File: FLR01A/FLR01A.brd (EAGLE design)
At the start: 30.5 x 30.5 mm, 10 parts, among them J1 M10SMD_MALE, J2 M10SMD_MALE

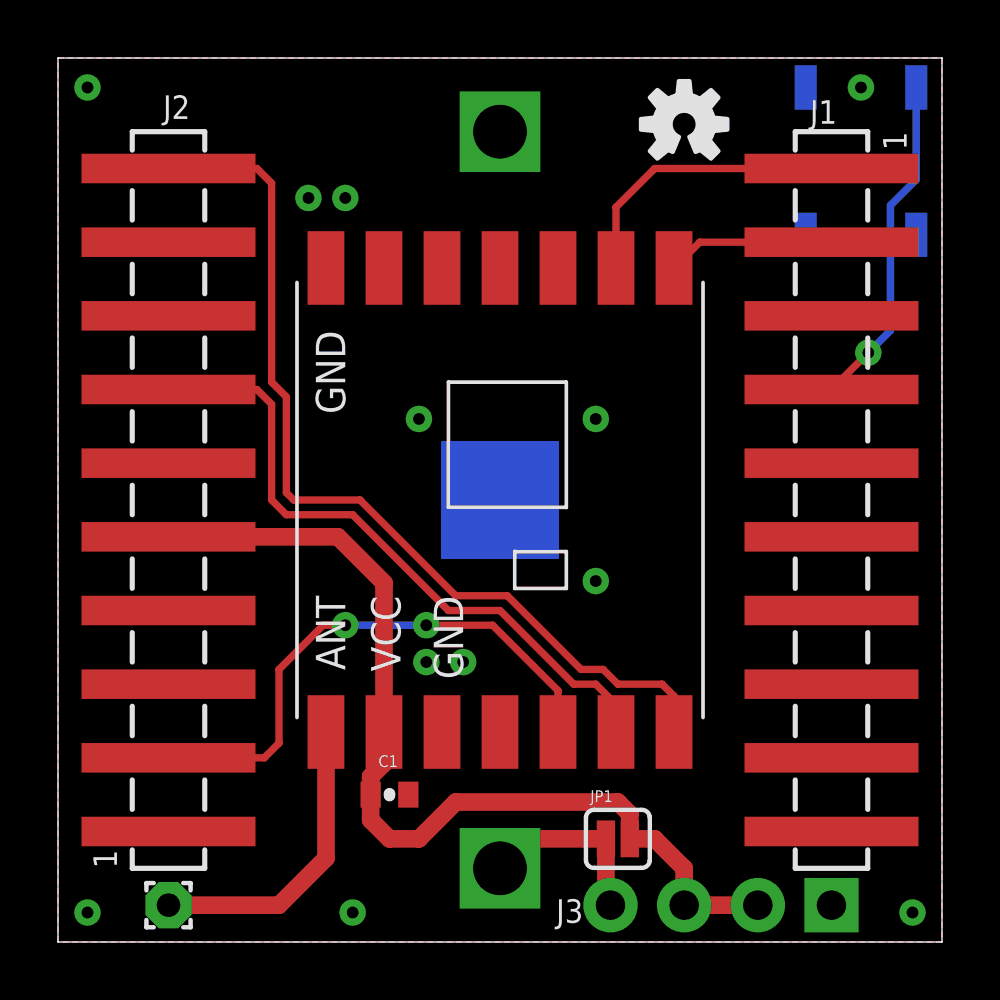
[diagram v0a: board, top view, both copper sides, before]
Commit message: [flr] add ptc fuse in series with battery
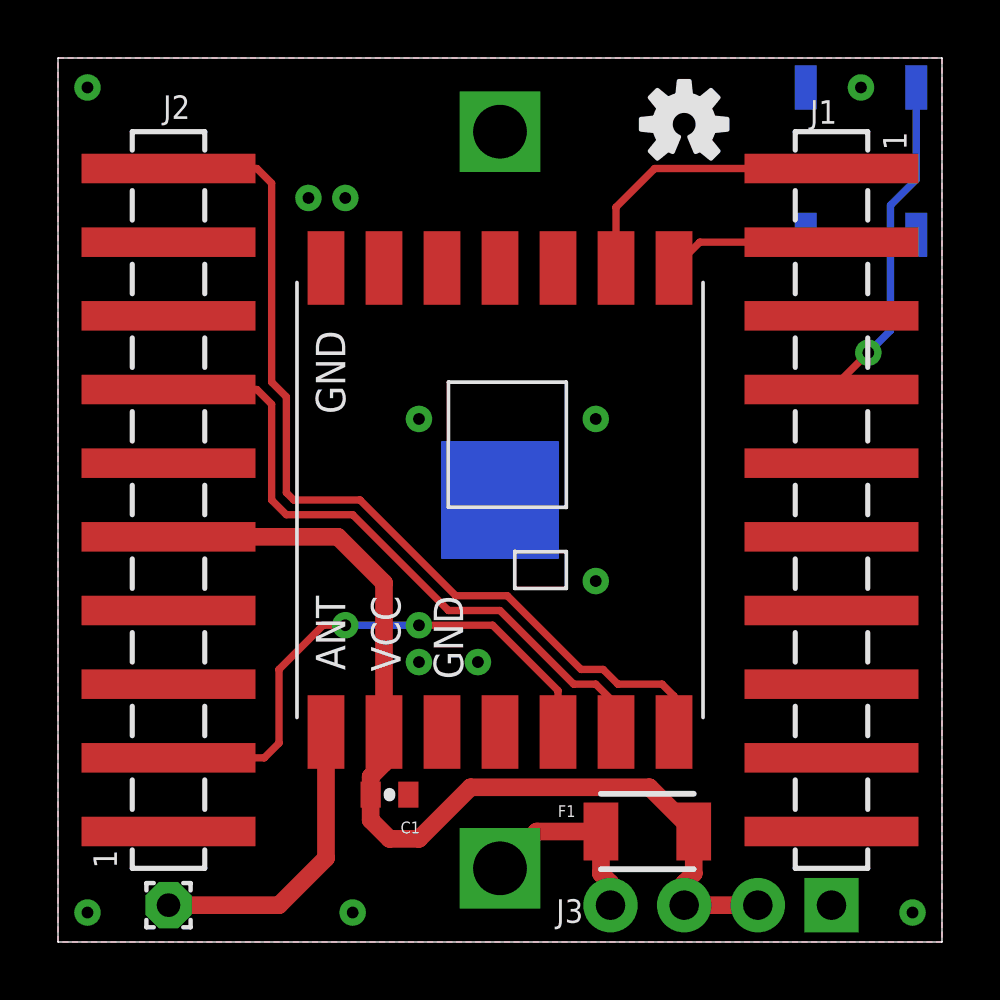
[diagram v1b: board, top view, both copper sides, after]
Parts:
- removed JP1: (no value), SparkFun-Passives:SJ_2S
- added F1: PTC1210, flukso:1210
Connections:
- net 3.3V: now also F1.2; no longer JP1.2
- net N$1: now also F1.1; no longer JP1.1
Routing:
- net 3.3V: track 33.3 -> 34.4 mm
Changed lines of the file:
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@@
 <element name="U$1" library="sparkFun" package="OSHW-LOGO-S" value="OSHW-LOGOS" x="21.59" y="28.194"/>
 <element name="C1" library="sparkFun" package="0402-CAP" value="100nF" x="11.43" y="5.08" smashed="yes">
-<attribute name="NAME" x="11.049" y="6.0325" size="0.4064" layer="25"/>
+<attribute name="NAME" x="11.811" y="3.7465" size="0.4064" layer="25"/>
 </element>
 <element name="U$5" library="flukso" package="RFM12B" value="RFM12B" x="15.24" y="15.24" smashed="yes" rot="R270"/>
@@
 </element>
 <element name="BAT1" library="SparkFun-Electromechanical" package="BATTCON_245MM_PTH" value="" x="15.24" y="15.24" smashed="yes" rot="MR270">
-<attribute name="NAME" x="14.605" y="18.161" size="0.4064" layer="26" rot="MR180"/>
 <attribute name="VALUE" x="15.875" y="24.765" size="0.4064" layer="28" rot="MR270"/>
 </element>
-<element name="JP1" library="SparkFun-Passives" package="SJ_2S" value="" x="19.304" y="3.556"/>
 <element name="J3" library="SparkFun-Connectors" package="1X04_NO_SILK" value="" x="26.67" y="1.27" smashed="yes" rot="R180">
 <attribute name="NAME" x="18.1102" y="1.4732" size="0.8128" layer="25" ratio="10" rot="R180"/>
@@
 <attribute name="PROD_ID" value="SWCH-08247" x="27.686" y="26.924" size="1.778" layer="28" rot="MR270" display="off"/>
 <attribute name="NAME" x="24.384" y="27.559" size="0.4064" layer="26" rot="MR90"/>
+</element>
+<element name="F1" library="flukso" package="1210" value="PTC1210" x="20.32" y="3.81" smashed="yes">
+<attribute name="NAME" x="17.234" y="4.31" size="0.4064" layer="25"/>
 </element>
 </elements>
@@
 <contactref element="BAT1" pad="2"/>
 <contactref element="J3" pad="1"/>
-<via x="12.7" y="9.652" extent="1-16" drill="0.4064" diameter="0.6096"/>
-<via x="13.97" y="9.652" extent="1-16" drill="0.4064" diameter="0.6096"/>
+<via x="12.446" y="9.652" extent="1-16" drill="0.4064" diameter="0.6096"/>
+<via x="14.478" y="9.652" extent="1-16" drill="0.4064" diameter="0.6096"/>
 <via x="8.636" y="25.654" extent="1-16" drill="0.4064" diameter="0.6096"/>
 <via x="9.906" y="25.654" extent="1-16" drill="0.4064" diameter="0.6096"/>
@@
 <contactref element="U$5" pad="VDD"/>
 <contactref element="C1" pad="1"/>
-<contactref element="JP1" pad="2"/>
 <contactref element="J3" pad="3"/>
 <contactref element="J3" pad="2"/>
-<wire x1="19.7159" y1="3.556" x2="19.7159" y2="4.4141" width="0.6096" layer="1"/>
-<wire x1="19.7159" y1="4.4141" x2="19.304" y2="4.826" width="0.6096" layer="1"/>
-<wire x1="19.304" y1="4.826" x2="13.716" y2="4.826" width="0.6096" layer="1"/>
-<wire x1="19.7159" y1="3.556" x2="20.574" y2="3.556" width="0.6096" layer="1"/>
-<wire x1="20.574" y1="3.556" x2="21.59" y2="2.54" width="0.6096" layer="1"/>
-<wire x1="21.59" y1="2.54" x2="21.59" y2="1.27" width="0.6096" layer="1"/>
 <wire x1="21.59" y1="1.27" x2="24.13" y2="1.27" width="0.6096" layer="1"/>
 <wire x1="11.24" y1="7.24" x2="11.24" y2="12.382" width="0.6096" layer="1"/>
 <wire x1="11.24" y1="12.382" x2="9.652" y2="13.97" width="0.6096" layer="1"/>
 <wire x1="9.652" y1="13.97" x2="3.81" y2="13.97" width="0.6096" layer="1"/>
-<wire x1="13.716" y1="4.826" x2="12.446" y2="3.556" width="0.6096" layer="1"/>
+<wire x1="14.224" y1="5.334" x2="12.446" y2="3.556" width="0.6096" layer="1"/>
 <wire x1="12.446" y1="3.556" x2="11.43" y2="3.556" width="0.6096" layer="1"/>
 <wire x1="11.43" y1="3.556" x2="10.78" y2="4.206" width="0.6096" layer="1"/>
@@
 <wire x1="10.78" y1="5.7" x2="11.24" y2="6.16" width="0.6096" layer="1"/>
 <wire x1="11.24" y1="6.16" x2="11.24" y2="7.24" width="0.6096" layer="1"/>
+<contactref element="F1" pad="2"/>
+<wire x1="21.92" y1="3.81" x2="21.92" y2="2.362" width="0.6096" layer="1"/>
+<wire x1="21.92" y1="2.362" x2="21.59" y2="2.032" width="0.6096" layer="1"/>
+<wire x1="21.59" y1="2.032" x2="21.59" y2="1.27" width="0.6096" layer="1"/>
+<wire x1="14.224" y1="5.334" x2="20.396" y2="5.334" width="0.6096" layer="1"/>
+<wire x1="20.396" y1="5.334" x2="21.92" y2="3.81" width="0.6096" layer="1"/>
 </signal>
 <signal name="N$6">
@@
 <wire x1="7.62" y1="6.858" x2="7.62" y2="9.398" width="0.254" layer="1"/>
 <via x="9.906" y="10.922" extent="1-16" drill="0.4064" diameter="0.6096"/>
-<wire x1="9.906" y1="10.922" x2="12.7" y2="10.922" width="0.254" layer="16"/>
-<via x="12.7" y="10.922" extent="1-16" drill="0.4064" diameter="0.6096"/>
+<wire x1="9.906" y1="10.922" x2="12.446" y2="10.922" width="0.254" layer="16"/>
+<via x="12.446" y="10.922" extent="1-16" drill="0.4064" diameter="0.6096"/>
 <wire x1="7.62" y1="9.398" x2="9.144" y2="10.922" width="0.254" layer="1"/>
 <wire x1="9.144" y1="10.922" x2="9.906" y2="10.922" width="0.254" layer="1"/>
-<wire x1="12.7" y1="10.922" x2="14.986" y2="10.922" width="0.254" layer="1"/>
+<wire x1="12.446" y1="10.922" x2="14.986" y2="10.922" width="0.254" layer="1"/>
 <wire x1="14.986" y1="10.922" x2="17.24" y2="8.668" width="0.254" layer="1"/>
 <wire x1="17.24" y1="8.668" x2="17.24" y2="7.24" width="0.254" layer="1"/>
@@
 <contactref element="BAT1" pad="3"/>
 <contactref element="J3" pad="4"/>
-<contactref element="JP1" pad="1"/>
-<wire x1="15.24" y1="2.54" x2="16.256" y2="3.556" width="0.6096" layer="1"/>
-<wire x1="16.256" y1="3.556" x2="18.8921" y2="3.556" width="0.6096" layer="1"/>
-<wire x1="18.8921" y1="3.556" x2="18.8921" y2="1.4279" width="0.6096" layer="1"/>
-<wire x1="18.8921" y1="1.4279" x2="19.05" y2="1.27" width="0.6096" layer="1"/>
+<contactref element="F1" pad="1"/>
+<wire x1="15.24" y1="2.54" x2="16.51" y2="3.81" width="0.6096" layer="1"/>
+<wire x1="16.51" y1="3.81" x2="18.72" y2="3.81" width="0.6096" layer="1"/>
+<wire x1="18.72" y1="3.81" x2="18.72" y2="2.362" width="0.6096" layer="1"/>
+<wire x1="18.72" y1="2.362" x2="19.05" y2="2.032" width="0.6096" layer="1"/>
+<wire x1="19.05" y1="2.032" x2="19.05" y2="1.27" width="0.6096" layer="1"/>
 </signal>
 </signals>

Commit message: [flr] improve pcb routing
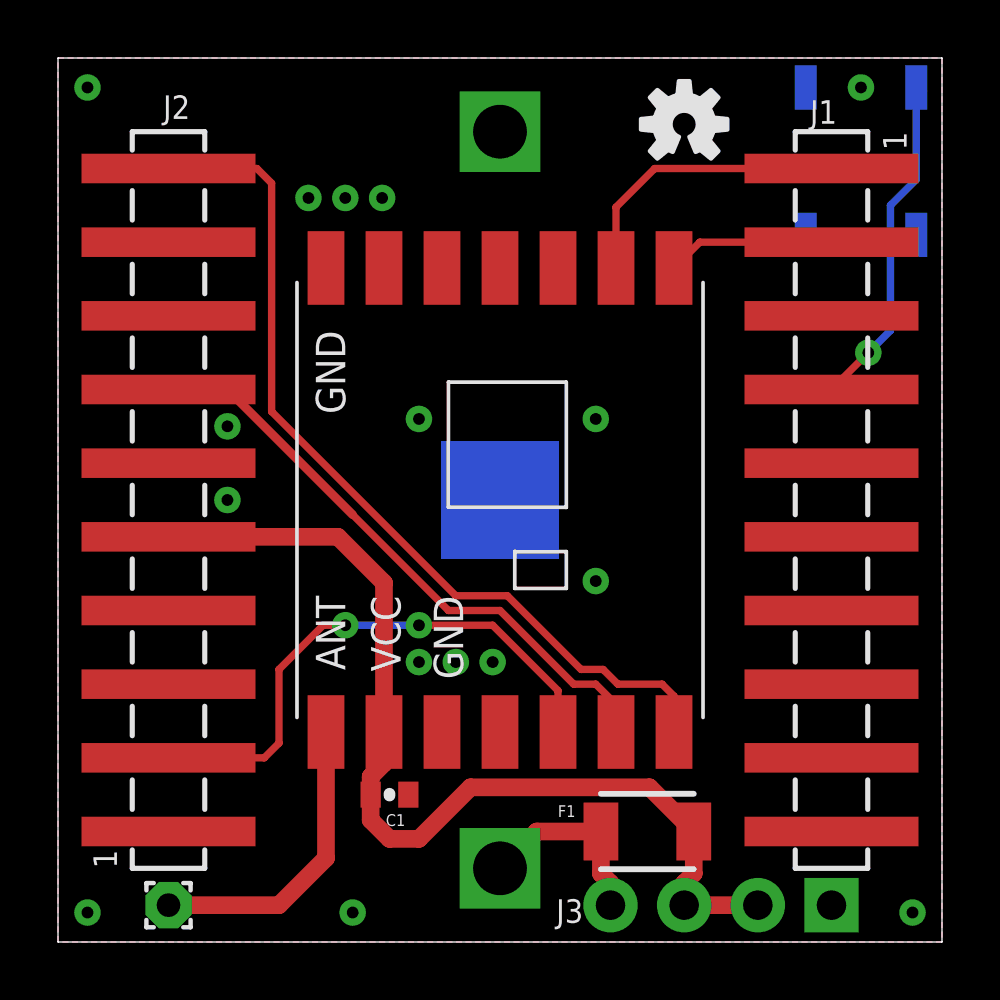
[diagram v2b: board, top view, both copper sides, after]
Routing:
- net PIO0_7: track 22.8 -> 20.9 mm
- net PIO0_14: track 32.2 -> 30.8 mm
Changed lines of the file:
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@@
 <element name="U$1" library="sparkFun" package="OSHW-LOGO-S" value="OSHW-LOGOS" x="21.59" y="28.194"/>
 <element name="C1" library="sparkFun" package="0402-CAP" value="100nF" x="11.43" y="5.08" smashed="yes">
-<attribute name="NAME" x="11.811" y="3.7465" size="0.4064" layer="25"/>
+<attribute name="NAME" x="11.303" y="4.0005" size="0.4064" layer="25"/>
 </element>
 <element name="U$5" library="flukso" package="RFM12B" value="RFM12B" x="15.24" y="15.24" smashed="yes" rot="R270"/>
@@
 <contactref element="J3" pad="1"/>
 <via x="12.446" y="9.652" extent="1-16" drill="0.4064" diameter="0.6096"/>
-<via x="14.478" y="9.652" extent="1-16" drill="0.4064" diameter="0.6096"/>
+<via x="13.716" y="9.652" extent="1-16" drill="0.4064" diameter="0.6096"/>
 <via x="8.636" y="25.654" extent="1-16" drill="0.4064" diameter="0.6096"/>
 <via x="9.906" y="25.654" extent="1-16" drill="0.4064" diameter="0.6096"/>
@@
 <via x="10.16" y="1.016" extent="1-16" drill="0.4064" diameter="0.6096"/>
 <contactref element="S1" pad="1"/>
+<via x="11.176" y="25.654" extent="1-16" drill="0.4064" diameter="0.6096"/>
+<via x="14.986" y="9.652" extent="1-16" drill="0.4064" diameter="0.6096"/>
+<via x="5.842" y="17.78" extent="1-16" drill="0.4064" diameter="0.6096"/>
+<via x="5.842" y="15.24" extent="1-16" drill="0.4064" diameter="0.6096"/>
 </signal>
 <signal name="3.3V">
@@
 <wire x1="3.81" y1="26.67" x2="6.858" y2="26.67" width="0.254" layer="1"/>
 <wire x1="6.858" y1="26.67" x2="7.366" y2="26.162" width="0.254" layer="1"/>
-<wire x1="7.366" y1="26.162" x2="7.366" y2="19.304" width="0.254" layer="1"/>
-<wire x1="7.366" y1="19.304" x2="7.874" y2="18.796" width="0.254" layer="1"/>
-<wire x1="7.874" y1="18.796" x2="7.874" y2="15.494" width="0.254" layer="1"/>
-<wire x1="7.874" y1="15.494" x2="8.128" y2="15.24" width="0.254" layer="1"/>
-<wire x1="8.128" y1="15.24" x2="10.414" y2="15.24" width="0.254" layer="1"/>
-<wire x1="10.414" y1="15.24" x2="13.716" y2="11.938" width="0.254" layer="1"/>
+<wire x1="7.366" y1="26.162" x2="7.366" y2="18.288" width="0.254" layer="1"/>
+<wire x1="7.366" y1="18.288" x2="13.716" y2="11.938" width="0.254" layer="1"/>
 <wire x1="13.716" y1="11.938" x2="15.494" y2="11.938" width="0.254" layer="1"/>
 <wire x1="15.494" y1="11.938" x2="18.034" y2="9.398" width="0.254" layer="1"/>
@@
 <contactref element="J2" pad="7"/>
 <contactref element="U$5" pad="SCK"/>
-<wire x1="3.81" y1="19.05" x2="6.858" y2="19.05" width="0.254" layer="1"/>
-<wire x1="6.858" y1="19.05" x2="7.366" y2="18.542" width="0.254" layer="1"/>
-<wire x1="7.366" y1="18.542" x2="7.366" y2="15.24" width="0.254" layer="1"/>
-<wire x1="7.366" y1="15.24" x2="7.874" y2="14.732" width="0.254" layer="1"/>
-<wire x1="7.874" y1="14.732" x2="10.16" y2="14.732" width="0.254" layer="1"/>
 <wire x1="10.16" y1="14.732" x2="13.462" y2="11.43" width="0.254" layer="1"/>
 <wire x1="13.462" y1="11.43" x2="15.24" y2="11.43" width="0.254" layer="1"/>
@@
 <wire x1="18.542" y1="8.89" x2="19.24" y2="8.192" width="0.254" layer="1"/>
 <wire x1="19.24" y1="8.192" x2="19.24" y2="7.24" width="0.254" layer="1"/>
+<wire x1="10.16" y1="14.732" x2="5.842" y2="19.05" width="0.3048" layer="1"/>
+<wire x1="5.842" y1="19.05" x2="3.81" y2="19.05" width="0.3048" layer="1"/>
 </signal>
 <signal name="PIO0_8">

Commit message: [flk/flr] introduce r3 of sensor and radio board
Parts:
- J1, J2: value M10SMD_MALE -> M10SMD_MALE_SHORT; device flukso:1X10_SMD_MALE -> flukso:1X10_SMD_MALE_SHORT
- moved PAD1 3.05 mm to (6.86, 1.27)
- moved S1 0.36 mm to (27.4, 26.7)
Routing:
- net N$6: track 10.5 -> 6.96 mm
- net PIO0_14: track 30.8 -> 27.8 mm
- net PIO0_7: track 20.9 -> 22.8 mm
- net PIO0_5: track 11.9 -> 13.5 mm
- net 3.3V: track 34.4 -> 36.0 mm
- net PIO0_17: track 10.1 -> 11.6 mm
- net PIO0_1: track 19.2 -> 17.8 mm
- net PIO0_13: track 5.80 -> 4.80 mm
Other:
- board text added: "18/02/15"
- board text added: "FLR01Ar3"
- board text removed: "15/11/14"
- board text removed: "FLR01Ar2"

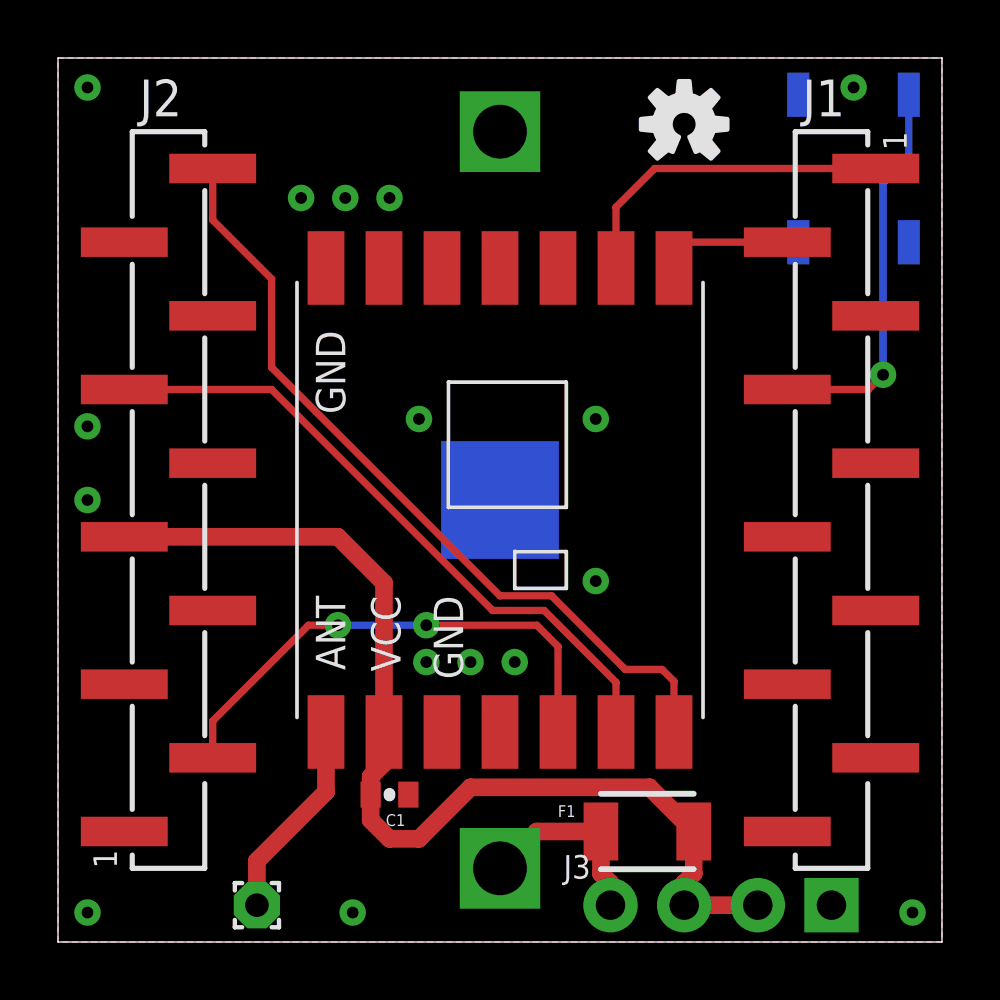
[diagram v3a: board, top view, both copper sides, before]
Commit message: [flk/flr] adapt board layout to new M10 footprints + power switch
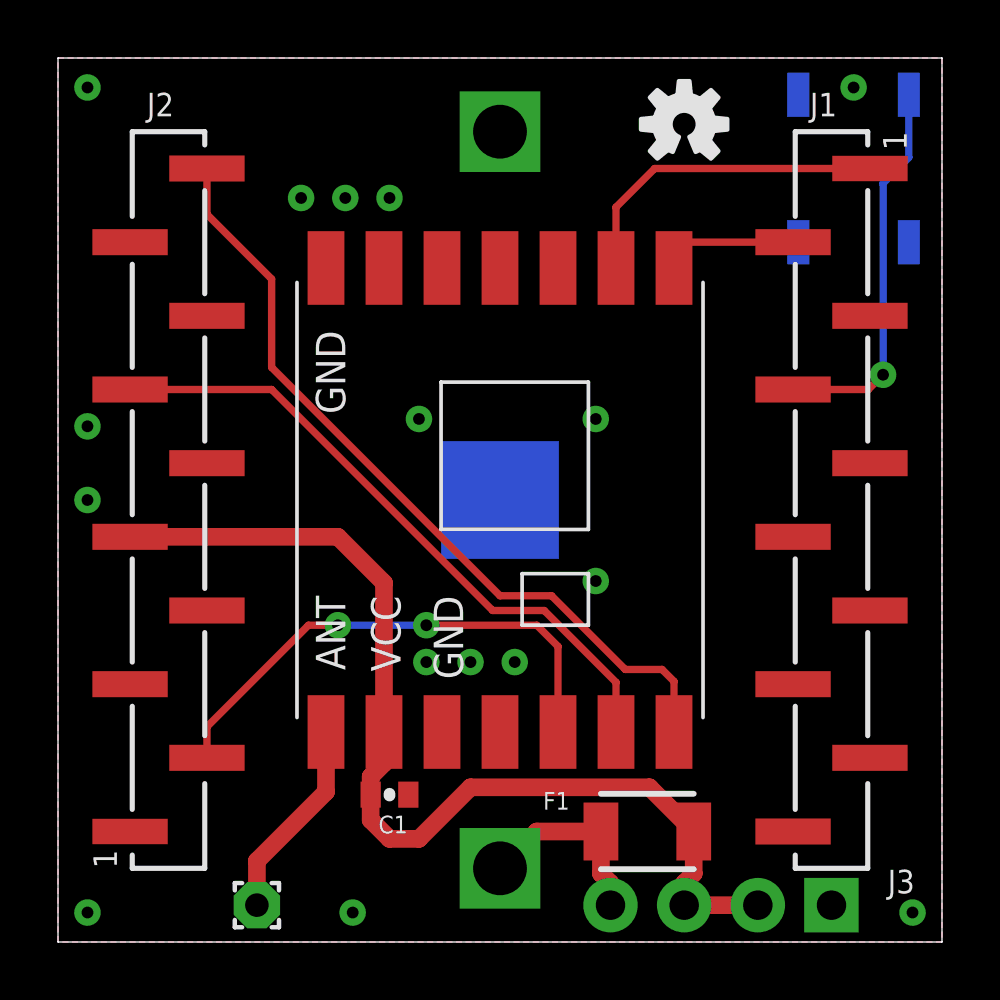
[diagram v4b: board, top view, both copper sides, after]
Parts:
- removed U$5: RFM12B, flukso:RFM12B
- added U$2: RFM69CW, flukso:RFM69CW
- J1, J2: value M10SMD_MALE_SHORT -> M10SMD_FEMALE_SHORT; device flukso:1X10_SMD_MALE_SHORT -> flukso:1X10_SMD_FEMALE_SHORT
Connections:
- net 3.3V: now also U$2.VDD; no longer U$5.VDD
- net GND: now also U$2.GND1, U$2.GND2; no longer U$5.GND1, U$5.GND2
- net N$6: now also U$2.ANT; no longer U$5.ANT
- net PIO0_1: now also U$2.SDI; no longer U$5.SDI
- net PIO0_13: now also U$2.SDO; no longer U$5.SDO
- net PIO0_14: now also U$2.SEL; no longer U$5.SEL
- net PIO0_17: now also U$2.IRQ; no longer U$5.IRQ
- net PIO0_7: now also U$2.SCK; no longer U$5.SCK
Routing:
- net PIO0_14: track 27.8 -> 28.5 mm
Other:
- board text added: "09/03/15"
- board text removed: "18/02/15"
